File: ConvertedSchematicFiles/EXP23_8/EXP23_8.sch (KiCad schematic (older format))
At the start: 28 parts, among them U1 uA741, U2 74393

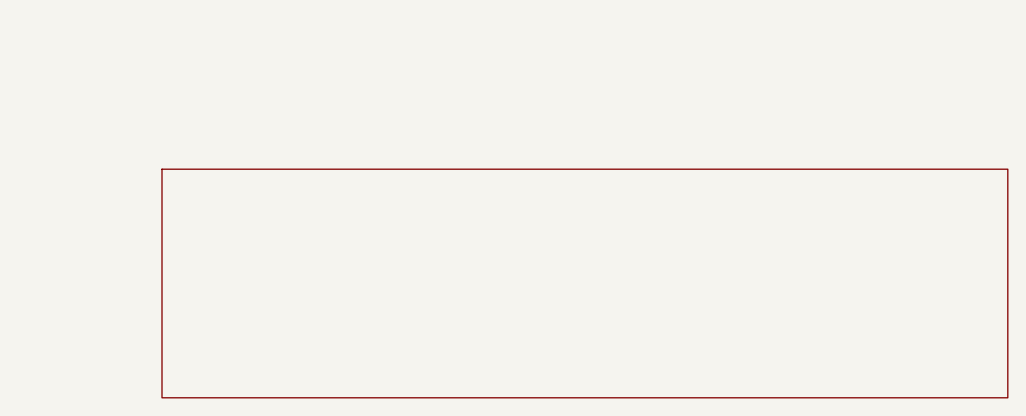
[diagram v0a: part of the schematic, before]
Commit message: Excluded some components. These no longer appear after conversion. When calling shell commands, filenames are in "quotes"
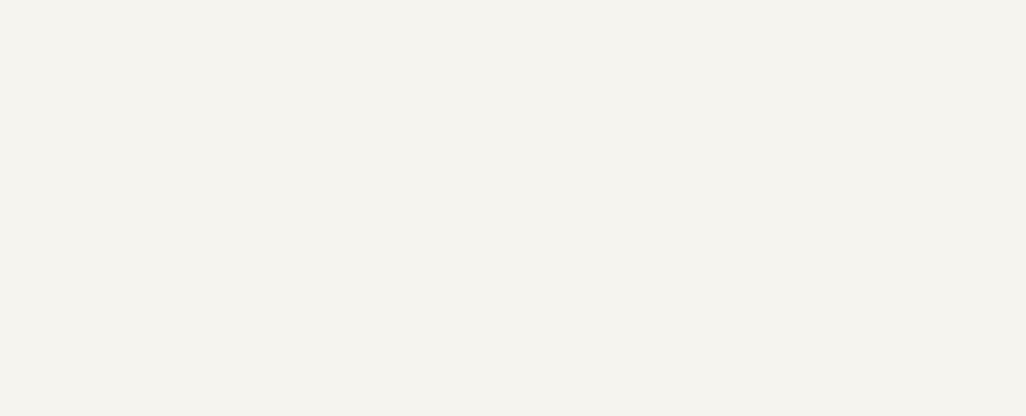
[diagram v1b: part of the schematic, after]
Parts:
- removed titleblk: titleblk, symbol TITLEBLK_PSPICE
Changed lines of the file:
@@
-	1    0    0    1
-$EndComp
-$Comp
-L TITLEBLK_PSPICE titleblk
-U 1 1 63665123
-P 9700 7200
-F 0 "titleblk" H 19400 14400 30  0001 L CNN
-F 1 "titleblk" H 19400 14480 30  0001 L CNN
-	1    9700 7200
 	1    0    0    1
 $EndComp

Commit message: Ports issue fixed. Now annotation for ports is #PWR? function added "itos"
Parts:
- removed EGND (x11): EGND, symbol EGND_PSPICE
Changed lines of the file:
@@
 $EndDescr
 $Comp
-L EGND_PSPICE EGND
+L EGND_PSPICE #PWR1
 U 1 1 14289383
 P 6600 2400
-F 0 "EGND" H 13200 4800 30  0001 L CNN
+F 0 "#PWR1" H 13200 4800 30  0001 L CNN
 F 1 "EGND" H 13200 4880 30  0001 L CNN
 	1    6600 2400
@@
 $EndComp
 $Comp
-L EGND_PSPICE EGND
+L EGND_PSPICE #PWR2
 U 1 1 46930886
 P 3600 2400
-F 0 "EGND" H 7200 4800 30  0001 L CNN
+F 0 "#PWR2" H 7200 4800 30  0001 L CNN
 F 1 "EGND" H 7200 4880 30  0001 L CNN
 	1    3600 2400
@@
 $EndComp
 $Comp
-L EGND_PSPICE EGND
+L EGND_PSPICE #PWR3
 U 1 1 71692777
 P 4500 2400
-F 0 "EGND" H 9000 4800 30  0001 L CNN
+F 0 "#PWR3" H 9000 4800 30  0001 L CNN
 F 1 "EGND" H 9000 4880 30  0001 L CNN
 	1    4500 2400
@@
 $EndComp
 $Comp
-L EGND_PSPICE EGND
+L EGND_PSPICE #PWR4
 U 1 1 14636915
 P 5400 2400
-F 0 "EGND" H 10800 4800 30  0001 L CNN
+F 0 "#PWR4" H 10800 4800 30  0001 L CNN
 F 1 "EGND" H 10800 4880 30  0001 L CNN
 	1    5400 2400
@@
 $EndComp
 $Comp
-L EGND_PSPICE EGND
+L EGND_PSPICE #PWR5
 U 1 1 77747793
 P 2700 2400
-F 0 "EGND" H 5400 4800 30  0001 L CNN
+F 0 "#PWR5" H 5400 4800 30  0001 L CNN
 F 1 "EGND" H 5400 4880 30  0001 L CNN
 	1    2700 2400
@@
 $EndComp
 $Comp
-L EGND_PSPICE EGND
+L EGND_PSPICE #PWR6
 U 1 1 74238335
 P 2400 2000
-F 0 "EGND" H 4800 4000 30  0001 L CNN
+F 0 "#PWR6" H 4800 4000 30  0001 L CNN
 F 1 "EGND" H 4800 4080 30  0001 L CNN
 	1    2400 2000
@@
 $EndComp
 $Comp
-L EGND_PSPICE EGND
+L EGND_PSPICE #PWR7
 U 1 1 99885386
 P 2200 3900
-F 0 "EGND" H 4400 7800 30  0001 L CNN
+F 0 "#PWR7" H 4400 7800 30  0001 L CNN
 F 1 "EGND" H 4400 7880 30  0001 L CNN
 	1    2200 3900
@@
 $EndComp
 $Comp
-L EGND_PSPICE EGND
+L EGND_PSPICE #PWR8
 U 1 1 39760492
 P 7700 3800
-F 0 "EGND" H 15400 7600 30  0001 L CNN
+F 0 "#PWR8" H 15400 7600 30  0001 L CNN
 F 1 "EGND" H 15400 7680 30  0001 L CNN
 	1    7700 3800
@@
 $EndComp
 $Comp
-L EGND_PSPICE EGND
+L EGND_PSPICE #PWR9
 U 1 1 66516649
 P 7000 3800
-F 0 "EGND" H 14000 7600 30  0001 L CNN
+F 0 "#PWR9" H 14000 7600 30  0001 L CNN
 F 1 "EGND" H 14000 7680 30  0001 L CNN
 	1    7000 3800
@@
 $EndComp
 $Comp
-L EGND_PSPICE EGND
+L EGND_PSPICE #PWR10
 U 1 1 29641421
 P 7400 1900
-F 0 "EGND" H 14800 3800 30  0001 L CNN
+F 0 "#PWR10" H 14800 3800 30  0001 L CNN
 F 1 "EGND" H 14800 3880 30  0001 L CNN
 	1    7400 1900
@@
 $EndComp
 $Comp
-L EGND_PSPICE EGND
+L EGND_PSPICE #PWR11
 U 1 1 45202362
 P 1500 3800
-F 0 "EGND" H 3000 7600 30  0001 L CNN
+F 0 "#PWR11" H 3000 7600 30  0001 L CNN
 F 1 "EGND" H 3000 7680 30  0001 L CNN
 	1    1500 3800

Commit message: Added LICENSE.txt
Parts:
- V4: value VPULSE -> PULSE
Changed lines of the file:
@@
 $EndDescr
 $Comp
-L EGND_PSPICE #PWR1
+L GND #PWR1
 U 1 1 14289383
 P 6600 2400
@@
 $EndComp
 $Comp
-L EGND_PSPICE #PWR2
+L GND #PWR2
 U 1 1 46930886
 P 3600 2400
@@
 $EndComp
 $Comp
-L EGND_PSPICE #PWR3
+L GND #PWR3
 U 1 1 71692777
 P 4500 2400
@@
 $EndComp
 $Comp
-L EGND_PSPICE #PWR4
+L GND #PWR4
 U 1 1 14636915
 P 5400 2400
@@
 $EndComp
 $Comp
-L EGND_PSPICE #PWR5
+L GND #PWR5
 U 1 1 77747793
 P 2700 2400
@@
 $EndComp
 $Comp
-L EGND_PSPICE #PWR6
+L GND #PWR6
 U 1 1 74238335
 P 2400 2000
@@
 $EndComp
 $Comp
-L EGND_PSPICE #PWR7
+L GND #PWR7
 U 1 1 99885386
 P 2200 3900
@@
 $EndComp
 $Comp
-L EGND_PSPICE #PWR8
+L GND #PWR8
 U 1 1 39760492
 P 7700 3800
@@
 $EndComp
 $Comp
-L EGND_PSPICE #PWR9
+L GND #PWR9
 U 1 1 66516649
 P 7000 3800
@@
 $EndComp
 $Comp
-L EGND_PSPICE #PWR10
+L GND #PWR10
 U 1 1 29641421
 P 7400 1900
@@
 $EndComp
 $Comp
-L EGND_PSPICE #PWR11
+L GND #PWR11
 U 1 1 45202362
 P 1500 3800
@@
 P 1500 3400
 F 0 "V4" H 1500 3400 30  0000 L CNN
-F 1 "VPULSE" H 1500 3480 30  0000 L CNN
+F 1 "PULSE" H 1500 3480 30  0000 L CNN
 	1    1500 3400
 	1    0    0    1

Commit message: Orientation fix. Library components are now inverted, with +ve y axis going up. In Schematic files, +ve y axis is downwards. This is how the KiCad libraries are. As a result of the above fixed, the converted GND is now oriented correctly.
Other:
- moved on the sheet: S1, S2, S3, S4, U1, U2, V2, V3, V4, VREF
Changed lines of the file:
@@
 F 1 "EGND" H 13200 4880 30  0001 L CNN
 	1    6600 2400
-	1    0    0    1
+	1    0    0    -1
 $EndComp
 $Comp
@@
 F 1 "EGND" H 7200 4880 30  0001 L CNN
 	1    3600 2400
-	1    0    0    1
+	1    0    0    -1
 $EndComp
 $Comp
@@
 F 1 "EGND" H 9000 4880 30  0001 L CNN
 	1    4500 2400
-	1    0    0    1
+	1    0    0    -1
 $EndComp
 $Comp
@@
 F 1 "EGND" H 10800 4880 30  0001 L CNN
 	1    5400 2400
-	1    0    0    1
+	1    0    0    -1
 $EndComp
 $Comp
@@
 F 1 "EGND" H 5400 4880 30  0001 L CNN
 	1    2700 2400
-	1    0    0    1
+	1    0    0    -1
 $EndComp
 $Comp
@@
 F 1 "EGND" H 4800 4080 30  0001 L CNN
 	1    2400 2000
-	1    0    0    1
+	1    0    0    -1
 $EndComp
 $Comp
@@
 F 1 "EGND" H 4400 7880 30  0001 L CNN
 	1    2200 3900
-	1    0    0    1
+	1    0    0    -1
 $EndComp
 $Comp
@@
 F 1 "EGND" H 15400 7680 30  0001 L CNN
 	1    7700 3800
-	1    0    0    1
+	1    0    0    -1
 $EndComp
 $Comp
@@
 F 1 "EGND" H 14000 7680 30  0001 L CNN
 	1    7000 3800
-	1    0    0    1
+	1    0    0    -1
 $EndComp
 $Comp
@@
 F 1 "EGND" H 14800 3880 30  0001 L CNN
 	1    7400 1900
-	1    0    0    1
+	1    0    0    -1
 $EndComp
 $Comp
@@
 F 1 "EGND" H 3000 7680 30  0001 L CNN
 	1    1500 3800
-	1    0    0    1
+	1    0    0    -1
 $EndComp
 $Comp
@@
 F 1 "Sbreak" H 2800 2380 30  0000 L CNN
 	1    2800 2300
-	1    0    0    1
+	1    0    0    -1
 $EndComp
 $Comp
@@
 F 1 "Sbreak" H 3700 2380 30  0000 L CNN
 	1    3700 2300
-	1    0    0    1
+	1    0    0    -1
 $EndComp
 $Comp
@@
 F 1 "Sbreak" H 4600 2380 30  0000 L CNN
 	1    4600 2300
-	1    0    0    1
+	1    0    0    -1
 $EndComp
 $Comp
@@
 F 1 "Sbreak" H 5500 2380 30  0000 L CNN
 	1    5500 2300
-	1    0    0    1
+	1    0    0    -1
 $EndComp
 $Comp
@@
 F 1 "R" H 7700 3480 30  0000 L CNN
 	1    7700 3400
-	0    -1    1    0
+	0    1    1    0
 $EndComp
 $Comp
@@
 F 1 "10K" H 3200 1890 30  0000 L CNN
 	1    3200 1600
-	0    -1    1    0
+	0    1    1    0
 $EndComp
 $Comp
@@
 F 1 "20k" H 4100 1910 30  0000 L CNN
 	1    4100 1600
-	0    -1    1    0
+	0    1    1    0
 $EndComp
 $Comp
@@
 F 1 "40K" H 5000 1910 30  0000 L CNN
 	1    5000 1600
-	0    -1    1    0
+	0    1    1    0
 $EndComp
 $Comp
@@
 F 1 "80k" H 5900 1890 30  0000 L CNN
 	1    5900 1600
-	0    -1    1    0
+	0    1    1    0
 $EndComp
 $Comp
@@
 F 1 "5k" H 7200 3350 30  0000 L CNN
 	1    7200 3200
-	1    0    0    1
+	1    0    0    -1
 $EndComp
 $Comp
@@
 F 1 "uA741" H 6600 2480 30  0000 L CNN
 	1    6600 2400
-	1    0    0    1
+	1    0    0    -1
 $EndComp
 $Comp
@@
 F 1 "15V" H 7000 3690 30  0000 C CNN
 	1    7000 3800
-	-1    0    0    -1
+	-1    0    0    1
 $EndComp
 $Comp
@@
 F 1 "15V" H 7400 1390 30  0000 C CNN
 	1    7400 1500
-	1    0    0    1
+	1    0    0    -1
 $EndComp
 $Comp
@@
 F 1 "74393" H 1900 3480 30  0000 L CNN
 	1    1900 3400
-	1    0    0    1
+	1    0    0    -1
 $EndComp
 $Comp
@@
 F 1 "PULSE" H 1500 3480 30  0000 L CNN
 	1    1500 3400
-	1    0    0    1
+	1    0    0    -1
 $EndComp
 $Comp
@@
 F 1 "-5V" H 2400 1490 30  0000 C CNN
 	1    2400 1600
-	1    0    0    1
+	1    0    0    -1
 $EndComp
 Wire Wire Line

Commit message: Removed the use of exec, wrote basename function, made integration with eSim easier.
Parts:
- added titleblk: titleblk, symbol titleblk_PSPICE
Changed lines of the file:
@@
-EESchema Schematic File Version 2  date Monday 16 August 1999 06:31:10 PM IST
+EESchema Schematic File Version 2  date
 LIBS:power
 LIBS:device
@@
 LIBS:contrib
 LIBS:valves
-LIBS:ConvertedSchematicFiles/EXP23_8-cache
 EELAYER 25  0
 EELAYER END
@@
 Sheet 1 1
 Title ""
-Date "16 Aug 1999"
+Date ""
 Rev ""
 Comp ""
@@
 	1    0    0    -1
 $EndComp
+$Comp
+L titleblk_PSPICE titleblk
+U 1 1 63665123
+P 9700 7200
+F 0 "titleblk" H 19400 14400 30  0001 L CNN
+F 1 "titleblk" H 19400 14480 30  0001 L CNN
+	1    9700 7200
+	1    0    0    -1
+$EndComp
